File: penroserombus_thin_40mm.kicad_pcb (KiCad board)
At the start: 2 copper layers, 72.4 x 23.5 mm, 21 parts, among them J1 Conn_01x03_Female, J2 Conn_01x03_Female, J3 Conn_01x03_Male, J4 Conn_01x03_Male, M2.1 MountingHole_2.1mm, SW1 SW_DPDT_x2

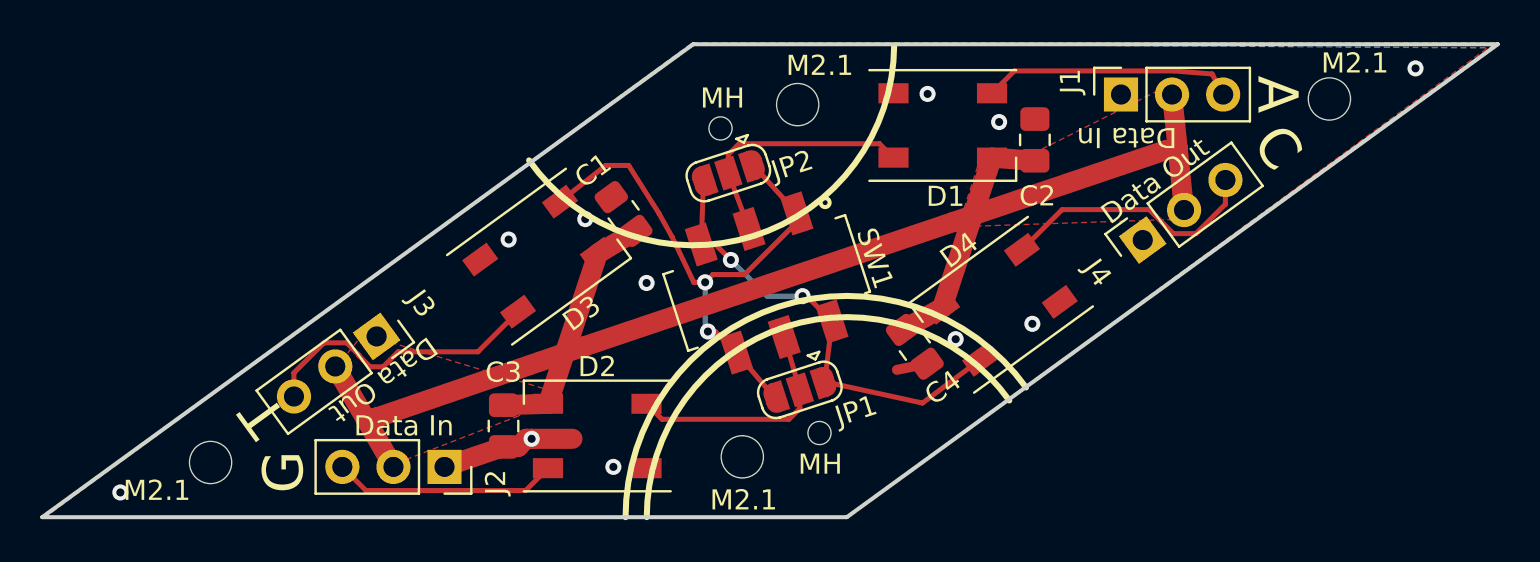
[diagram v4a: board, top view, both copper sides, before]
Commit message: increased mounting hole size to M3
increased mounting hole size to M3 to accomidate plastic adhesive mounting hole standoffs. makes the silkscreen a bit cramped and the VCC   route a bit long, but maybe I will make the top pour VCC instead of ground later idk.
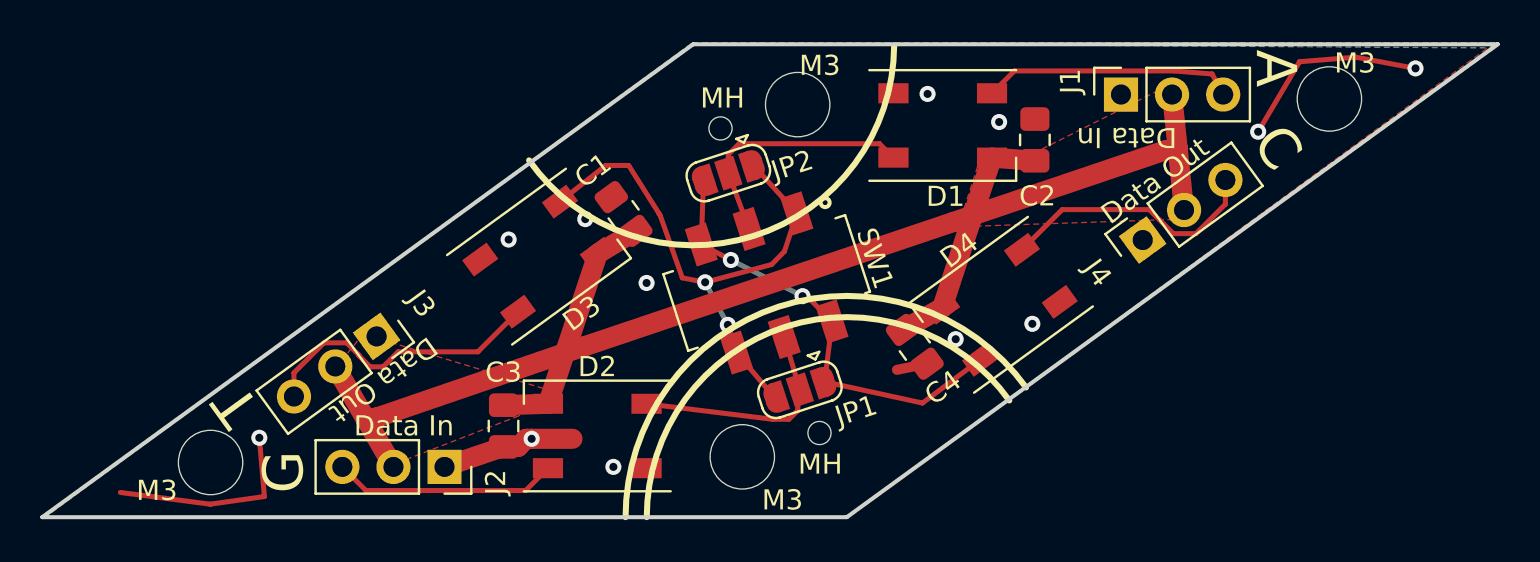
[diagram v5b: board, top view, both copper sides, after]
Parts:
- removed M2.1 (x2): MountingHole_2.1mm, MountingHole:MountingHole_2.1mm
- added M3: MountingHole_3.2mm_M3_ISO7380, MountingHole:MountingHole_3.2mm_M3_ISO7380, F.Cu at (153.6, 82.1)
- added M3: MountingHole_3.2mm_M3_ISO7380, MountingHole:MountingHole_3.2mm_M3_ISO7380, F.Cu at (156.4, 64.5)
- M3 (x2): renamed from M2.1; value MountingHole_2.1mm -> MountingHole_3.2mm_M3_ISO7380; footprint MountingHole:MountingHole_2.1mm -> MountingHole:MountingHole_3.2mm_M3_ISO7380
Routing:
- net GND: track 8.22 -> 28.3 mm, vias 11 -> 12

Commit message: board wiring changes and mounting hole additions for adhesive standoffs
changed top copper fill to VCC and added mounting holes with new footprint to check if the mounts collided.
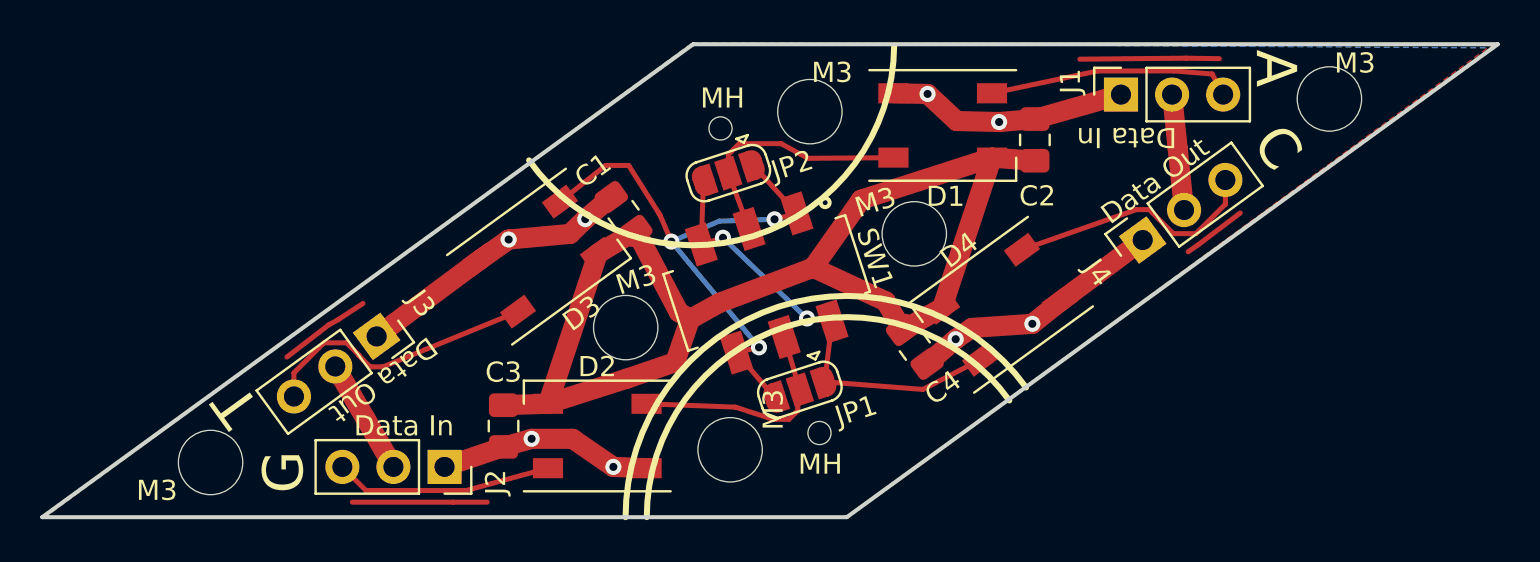
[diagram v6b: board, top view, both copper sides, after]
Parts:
- removed the M3 at (153.6, 82.1)
- removed the M3 at (156.4, 64.5)
- added M3: HC-5Nylonadhesiveclip, penroserombus:HC-5Nylonadhesiveclip, F.Cu at (162.2, 71.0)
- added M3: HC-5Nylonadhesiveclip, penroserombus:HC-5Nylonadhesiveclip, F.Cu at (147.8, 75.6)
- added M3: MountingHole_3.2mm_M3_ISO7380, MountingHole:MountingHole_3.2mm_M3_ISO7380, F.Cu at (153.0, 81.7)
- added M3: MountingHole_3.2mm_M3_ISO7380, MountingHole:MountingHole_3.2mm_M3_ISO7380, F.Cu at (157.0, 64.9)
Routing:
- net GND: track 28.3 -> 49.4 mm, vias 12 -> 8
- net VCC: track 78.6 -> 95.0 mm
- net Net-(D3-Pad2): track 27.8 -> 29.1 mm, vias 2 -> 3
- net Net-(D3-Pad4): track 14.6 -> 14.0 mm
- removed copper zone on F.Cu, net GND

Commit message: minor tweaks and diagrams
Tweaks to silkscreen and stuff also added a diagram to explain switch on board. Also made top layer VCC on penrose kite.
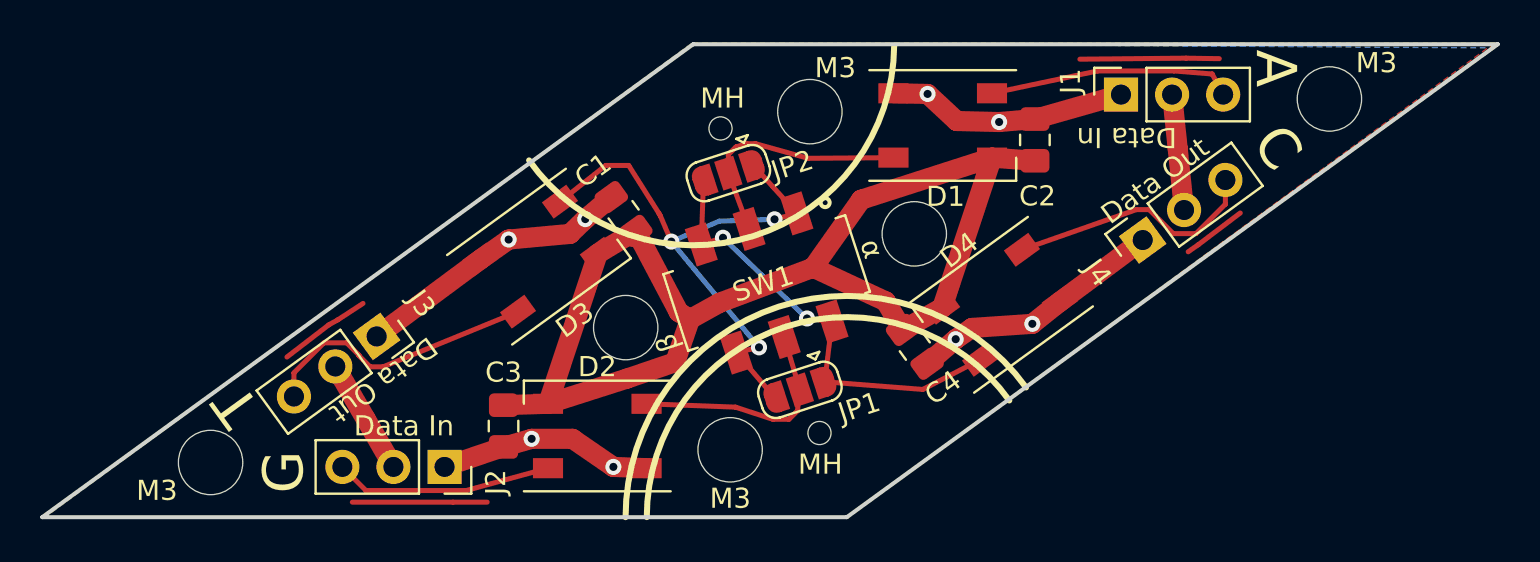
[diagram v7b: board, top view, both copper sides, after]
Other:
- board text added: "α"
- board text added: "β"
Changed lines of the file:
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@@
   (general
     (thickness 1.6)
-    (drawings 33)
-    (tracks 116)
+    (drawings 35)
+    (tracks 117)
     (zones 0)
     (modules 23)
@@
     (at 162.152501 70.963609 18)
     (zone_connect 2)
-    (fp_text reference M3 (at -1.349468 -2.090115 18) (layer F.SilkS)
-      (effects (font (size 1 1) (thickness 0.15)))
+    (fp_text reference M3 (at -0.184682 -2.502185 18) (layer B.SilkS)
+      (effects (font (size 1 1) (thickness 0.15)) (justify mirror))
     )
     (fp_text value HC-5Nylonadhesiveclip (at 0.1 -7.2 18) (layer F.Fab)
@@
   (module penroserombus:HC-5Nylonadhesiveclip (layer F.Cu)
     (at 147.806268 75.624982 18)
-    (fp_text reference M3 (at 1.240527 -2.103701 18) (layer F.SilkS)
-      (effects (font (size 1 1) (thickness 0.15)))
+    (fp_text reference M3 (at -0.411138 -2.659054 18) (layer B.SilkS)
+      (effects (font (size 1 1) (thickness 0.15)) (justify mirror))
     )
     (fp_text value HC-5Nylonadhesiveclip (at 0.1 -7.2 18) (layer F.Fab)
@@
     (tags "mounting hole 3.2mm no annular m3 iso7380")
     (attr virtual)
-    (fp_text reference M3 (at 1.997507 2.150999 90) (layer F.SilkS)
+    (fp_text reference M3 (at -2.419719 0.007845 180) (layer F.SilkS)
       (effects (font (size 1 1) (thickness 0.15)))
     )
@@
     (tags "mounting hole 3.2mm no annular m3 iso7380")
     (attr virtual)
-    (fp_text reference M3 (at 1.27 -1.778) (layer F.SilkS)
+    (fp_text reference M3 (at 2.340013 -1.79426) (layer F.SilkS)
       (effects (font (size 1 1) (thickness 0.15)))
     )
@@
     (tags "mounting hole 3.2mm no annular m3 iso7380")
     (attr virtual)
-    (fp_text reference M3 (at 1.101658 -1.939651) (layer F.SilkS)
+    (fp_text reference M3 (at 1.264665 -2.17599) (layer F.SilkS)
       (effects (font (size 1 1) (thickness 0.15)))
     )
@@
   (module penroserombus:Aliexpress_slideswitch_2P2T (layer F.Cu)
     (at 154.813 73.406 288)
-    (fp_text reference SW1 (at 0.5 -5.5 108) (layer F.SilkS)
+    (fp_text reference SW1 (at -0.022693 0.184918 198) (layer F.SilkS)
       (effects (font (size 1 1) (thickness 0.15)))
     )
@@
     (tags "LED RGB NeoPixel")
     (attr smd)
-    (fp_text reference D3 (at 0.066428 3.525804 36) (layer F.SilkS)
+    (fp_text reference D3 (at -0.40531 3.589836 36) (layer F.SilkS)
       (effects (font (size 1 1) (thickness 0.15)))
     )
@@
     (tags "solder jumper open")
     (attr virtual)
-    (fp_text reference JP1 (at -2.336887 -1.849375 18) (layer F.SilkS)
+    (fp_text reference JP1 (at -2.532062 -1.741865 18) (layer F.SilkS)
       (effects (font (size 1 1) (thickness 0.15)))
     )
@@
     (pad 2 smd rect (at 0 0 198) (size 1 1.5) (layers F.Cu F.Mask)
       (net 4 "Net-(D1-Pad4)"))
+  )
+  (gr_text β (at 149.87016 76.38288 108) (layer F.SilkS)
+    (effects (font (size 1 1) (thickness 0.15)))
+  )
+  (gr_text α (at 160.03016 71.70928 288) (layer F.SilkS)
+    (effects (font (size 1 1) (thickness 0.15)))
   )
   (gr_text "Gnd\nVcc\nData" (at 135.4074 79.756 288) (layer B.SilkS)
@@
   (segment (start 171.273611 62.863589) (end 175.064723 62.863589) (width 0.25) (layer F.Cu) (net 3))
   (segment (start 152.908 67.945) (end 153.940027 70.719265) (width 0.25) (layer F.Cu) (net 4))
-  (segment (start 152.908 67.021838) (end 153.449237 66.480601) (width 0.25) (layer F.Cu) (net 4))
   (segment (start 152.908 67.945) (end 152.908 67.021838) (width 0.25) (layer F.Cu) (net 4))
-  (segment (start 153.449237 66.480601) (end 155.533001 66.480601) (width 0.25) (layer F.Cu) (net 4))
-  (segment (start 155.533001 66.480601) (end 156.8704 67.2084) (width 0.25) (layer F.Cu) (net 4))
   (segment (start 156.8704 67.2084) (end 161.116375 67.176046) (width 0.25) (layer F.Cu) (net 4))
+  (segment (start 156.8704 67.2084) (end 154.257921 66.480601) (width 0.25) (layer F.Cu) (net 4))
+  (segment (start 153.287159 66.642679) (end 153.805801 66.480601) (width 0.25) (layer F.Cu) (net 4))
+  (segment (start 153.805801 66.480601) (end 154.257921 66.480601) (width 0.25) (layer F.Cu) (net 4))
+  (segment (start 152.908 67.021838) (end 153.287159 66.642679) (width 0.25) (layer F.Cu) (net 4))
   (segment (start 155.685973 76.092735) (end 156.464 78.719278) (width 0.25) (layer F.Cu) (net 5))
   (segment (start 156.34372 79.76272) (end 155.922763 80.183677) (width 0.25) (layer F.Cu) (net 5))
